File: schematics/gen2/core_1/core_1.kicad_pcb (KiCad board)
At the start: 2 copper layers, 84.3 x 8.4 mm, 10 parts, among them U1 74LS00, U2 74LS04, U3 74LS109, U4 74LS02

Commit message: core1 completed
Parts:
- added C1: C, Capacitor_THT:C_Disc_D5.0mm_W2.5mm_P2.50mm, F.Cu at (191.0, 79.2)
- added C10: C, Capacitor_THT:C_Disc_D5.0mm_W2.5mm_P2.50mm, F.Cu at (173.0, 38.2)
- added C11: C, Capacitor_THT:C_Disc_D5.0mm_W2.5mm_P2.50mm, F.Cu at (122.0, 71.7)
- added C12: C, Capacitor_THT:C_Disc_D5.0mm_W2.5mm_P2.50mm, F.Cu at (106.5, 71.4)
- added C16: C, Capacitor_THT:C_Disc_D5.0mm_W2.5mm_P2.50mm, F.Cu at (145.2, 102.8)
- added C2: C, Capacitor_THT:C_Disc_D5.0mm_W2.5mm_P2.50mm, F.Cu at (175.4, 78.3)
- added C3: C, Capacitor_THT:C_Disc_D5.0mm_W2.5mm_P2.50mm, F.Cu at (190.4, 52.9)
- added C4: C, Capacitor_THT:C_Disc_D5.0mm_W2.5mm_P2.50mm, F.Cu at (142.6, 39.0)
- added C5: C, Capacitor_THT:C_Radial_D6.3mm_H5.0mm_P2.50mm, F.Cu at (105.0, 117.5)
- added C9: C, Capacitor_THT:C_Disc_D5.0mm_W2.5mm_P2.50mm, F.Cu at (157.8, 39.5)
- added R1: 5kOhm, Resistor_THT:R_Axial_DIN0207_L6.3mm_D2.5mm_P7.62mm_Horizontal, F.Cu at (179.2, 102.6)
- moved INSTRUCTION1 72.1 mm to (144.6, 113.6), turned to 90 degrees
- moved DECODER2 70.2 mm to (161.4, 38.4)
- moved DECODER1 67.3 mm to (146.8, 38.4)
- moved U1 64.2 mm to (182.9, 57.0)
- moved U4 60.5 mm to (167.8, 82.2)
- moved U3 58.3 mm to (182.9, 82.4)
- moved DECODER4 54.5 mm to (98.9, 75.7)
- moved DECODER3 52.6 mm to (114.4, 75.7)
- moved BC1 47.9 mm to (103.0, 126.5)
- moved U2 16.8 mm to (130.9, 38.4)
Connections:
- U4 pad 11: Net-(R2-Pad2) -> Net-(U3A-~{S})
- U4 pad 12: Net-(R2-Pad2) -> Net-(U3A-~{S})
- U4 pad 8: Net-(R2-Pad2) -> Net-(U3A-~{S})
- U4 pad 9: Net-(R2-Pad2) -> Net-(U3A-~{S})
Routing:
- net /~{IntAck}: track 0.00 -> 277.5 mm, vias 0 -> 5
- net /~{ALUWriter}: track 0.00 -> 270.8 mm, vias 0 -> 5
- net /R4: track 0.00 -> 217.5 mm, vias 0 -> 5
- net Net-(DECODER3-E1): track 0.00 -> 164.7 mm, vias 0 -> 2
- net GND: track 0.00 -> 151.6 mm, vias 0 -> 7
- net /L0: track 0.00 -> 111.3 mm, vias 0 -> 2
- net Net-(BC1-STATE15): track 0.00 -> 110.6 mm, vias 0 -> 7
- net /L1: track 0.00 -> 108.5 mm, vias 0 -> 2
- net /~{InstructionReader}: track 0.00 -> 107.1 mm
- net /L2: track 0.00 -> 105.2 mm, vias 0 -> 2
- net /L3: track 0.00 -> 102.4 mm, vias 0 -> 2
- net /~{MemoryReader}: track 0.00 -> 101.4 mm, vias 0 -> 2
- net /IRQ: track 0.00 -> 94.5 mm, vias 0 -> 3
- net /SPHighReader: track 0.00 -> 92.1 mm, vias 0 -> 4
- net /STATE1: track 0.00 -> 89.8 mm, vias 0 -> 1
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- added copper zone on B.Cu, net GND
- added copper zone on F.Cu, net VCC
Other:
- board size 84.3 x 8.4 mm -> 100 x 91.1 mm

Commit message: design + fix core_2
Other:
- board text added: "CORE 2"

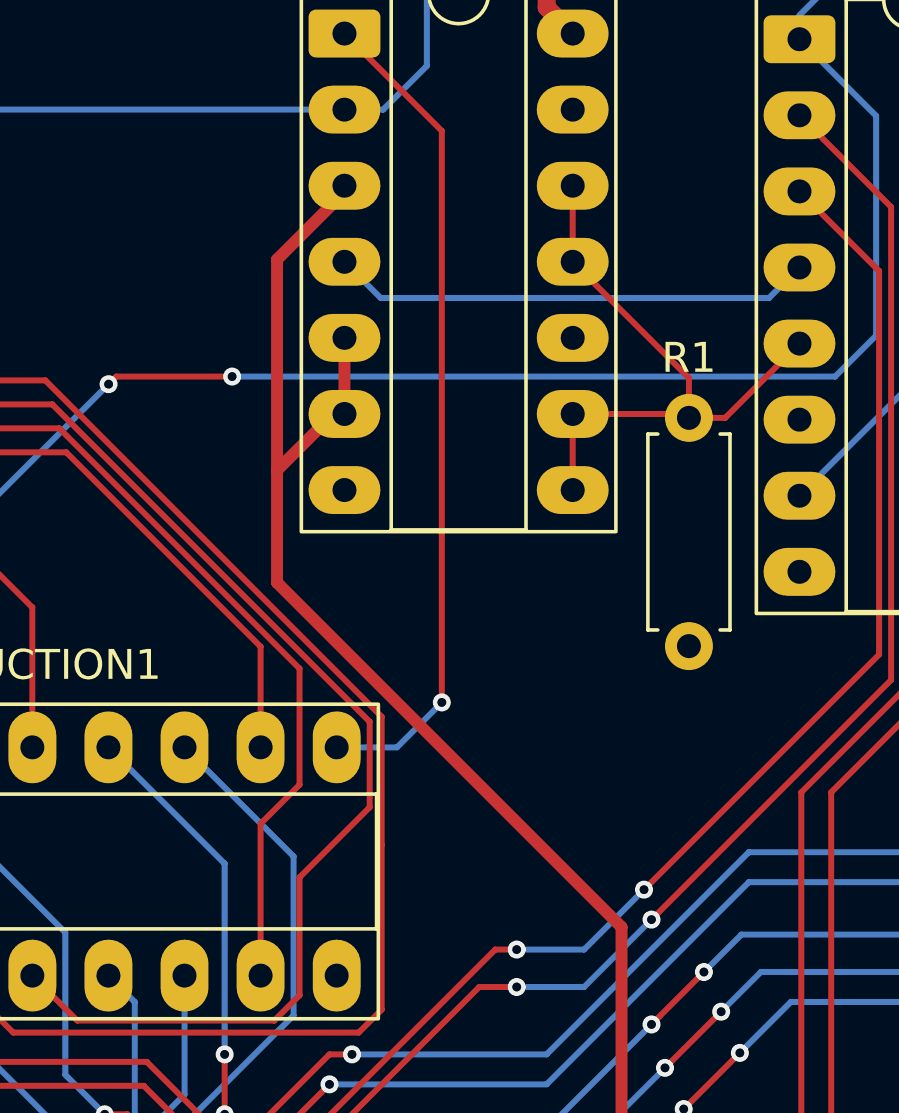
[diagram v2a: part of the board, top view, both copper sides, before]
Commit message: fix clk in core_1
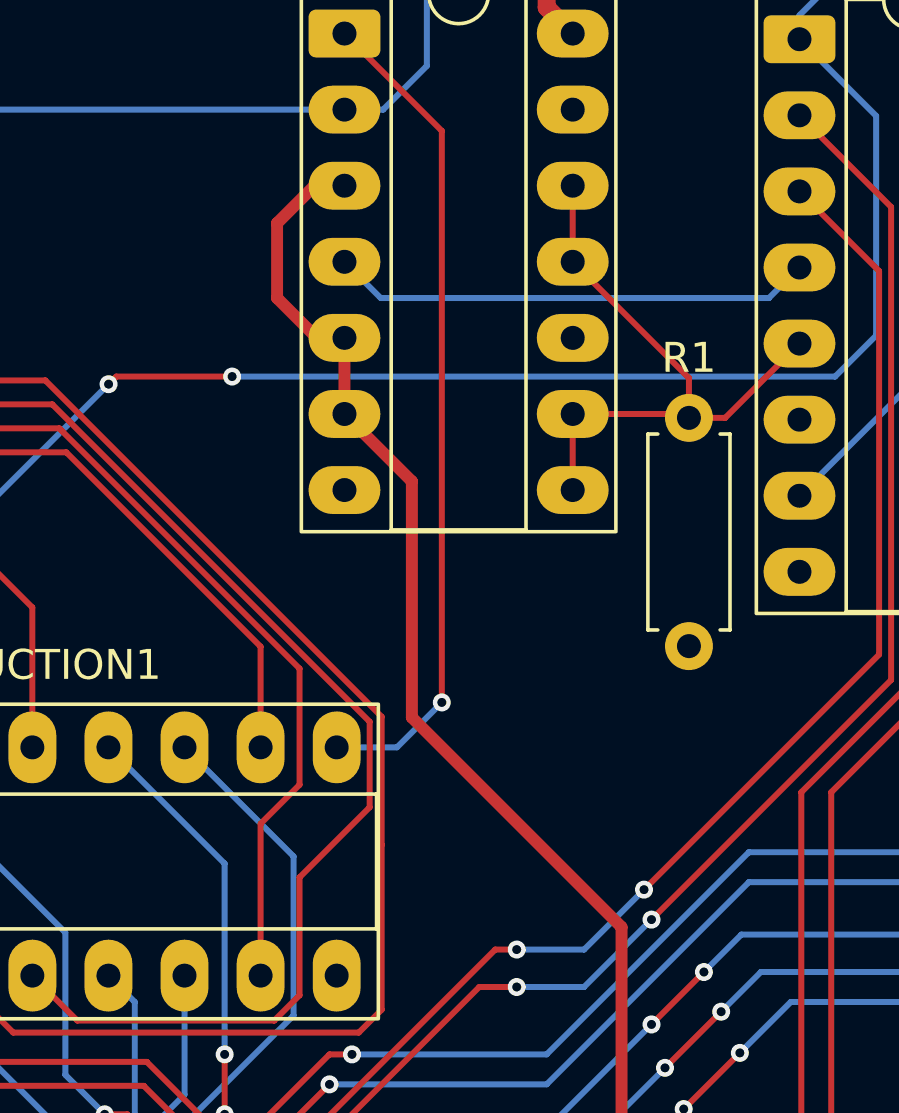
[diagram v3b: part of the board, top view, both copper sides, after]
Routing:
- net /~{Clk}: track 50.4 -> 46.4 mm
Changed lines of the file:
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@@
 	)
 	(segment
-		(start 165.5 89.713125)
-		(end 167.84472 87.368405)
+		(start 170 105)
+		(end 170 97.12)
 		(width 0.4)
 		(layer "F.Cu")
@@
 	)
 	(segment
-		(start 165.5 100.5)
-		(end 165.5 96.75)
+		(start 166.83 92.33)
+		(end 167.75 92.33)
 		(width 0.4)
 		(layer "F.Cu")
@@
 	)
 	(segment
-		(start 165.5 96.75)
-		(end 165.5 89.713125)
+		(start 165.5 88.5)
+		(end 165.5 91)
+		(width 0.4)
+		(layer "F.Cu")
+		(net 38)
+	)
+	(segment
+		(start 177 126.5)
+		(end 177 112)
+		(width 0.4)
+		(layer "F.Cu")
+		(net 38)
+	)
+	(segment
+		(start 167.75 87.25)
+		(end 166.75 87.25)
 		(width 0.4)
 		(layer "F.Cu")
@@
 	)
 	(segment
+		(start 165.5 91)
+		(end 166.83 92.33)
+		(width 0.4)
+		(layer "F.Cu")
+		(net 38)
+	)
+	(segment
+		(start 177 112)
+		(end 170 105)
+		(width 0.4)
+		(layer "F.Cu")
+		(net 38)
+	)
+	(segment
 		(start 167.75 94.87)
 		(end 167.75 92.33)
@@
 	)
 	(segment
-		(start 177 112)
-		(end 165.5 100.5)
+		(start 166.75 87.25)
+		(end 165.5 88.5)
 		(width 0.4)
 		(layer "F.Cu")
@@
 	)
 	(segment
-		(start 165.5 96.75)
-		(end 167.38 94.87)
+		(start 170 97.12)
+		(end 167.75 94.87)
 		(width 0.4)
 		(layer "F.Cu")
-		(net 38)
-	)
-	(segment
-		(start 177 126.5)
-		(end 177 112)
-		(width 0.4)
-		(layer "F.Cu")

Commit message: chore(core 1): added logo and text
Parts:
- added kibuzzard-6911CC41: G***, kibuzzard-6911CC41, F.Cu at (102.0, 35.6)
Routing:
- net VCC: track 61.7 -> 89.7 mm
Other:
- board text removed: "CORE 2"

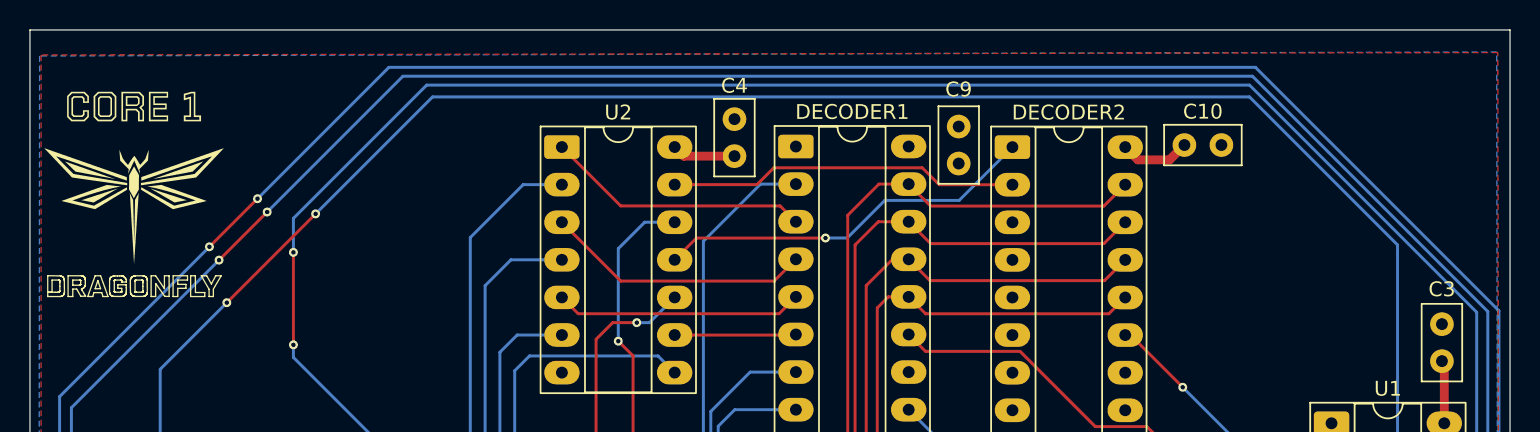
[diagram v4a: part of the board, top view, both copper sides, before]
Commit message: chore(kicad-pcb): added apps ucu logo
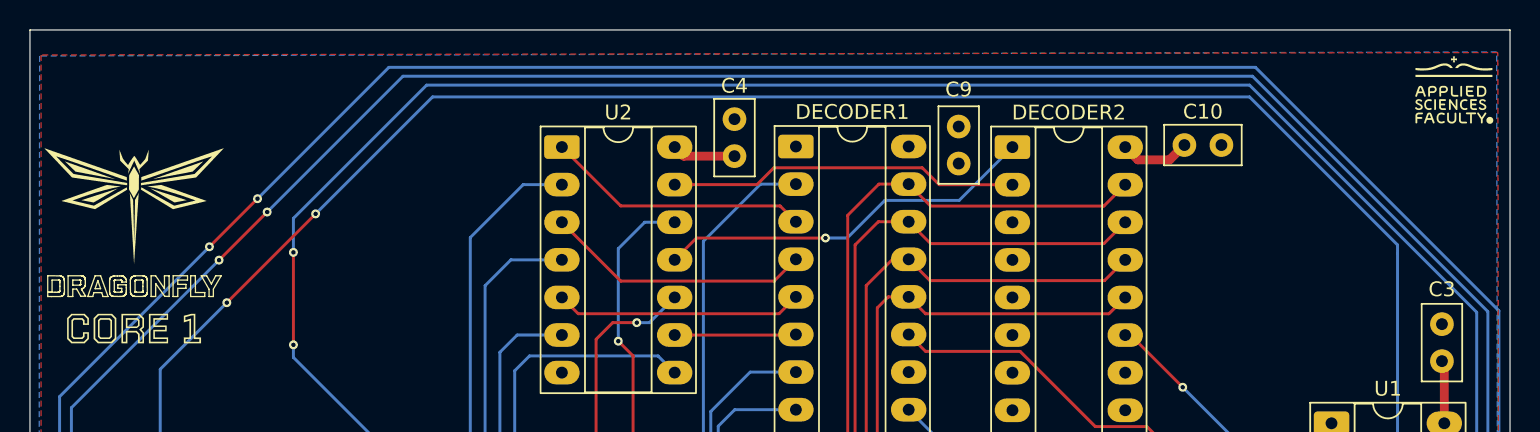
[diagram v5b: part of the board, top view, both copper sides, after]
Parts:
- moved kibuzzard-6911CC41 15.0 mm to (102.0, 50.6)

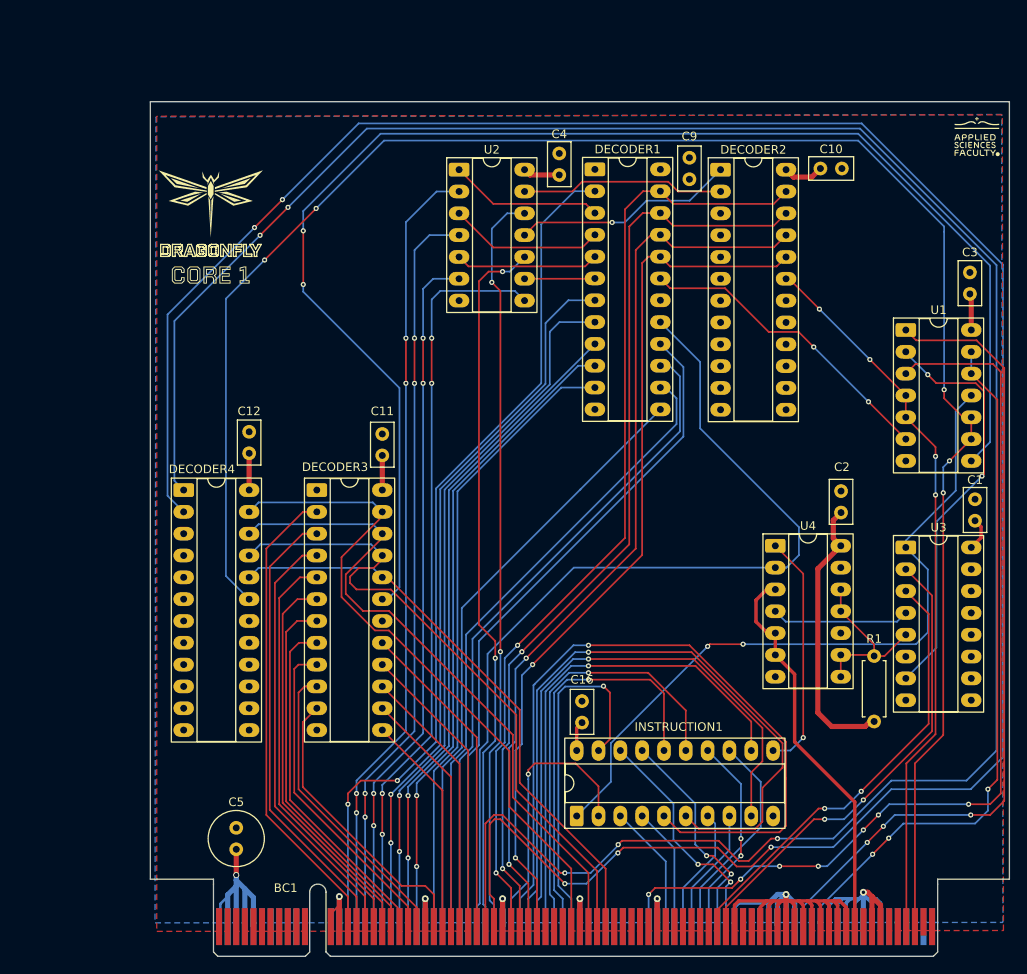
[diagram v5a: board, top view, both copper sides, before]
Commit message: fix(kicad): vcc zones
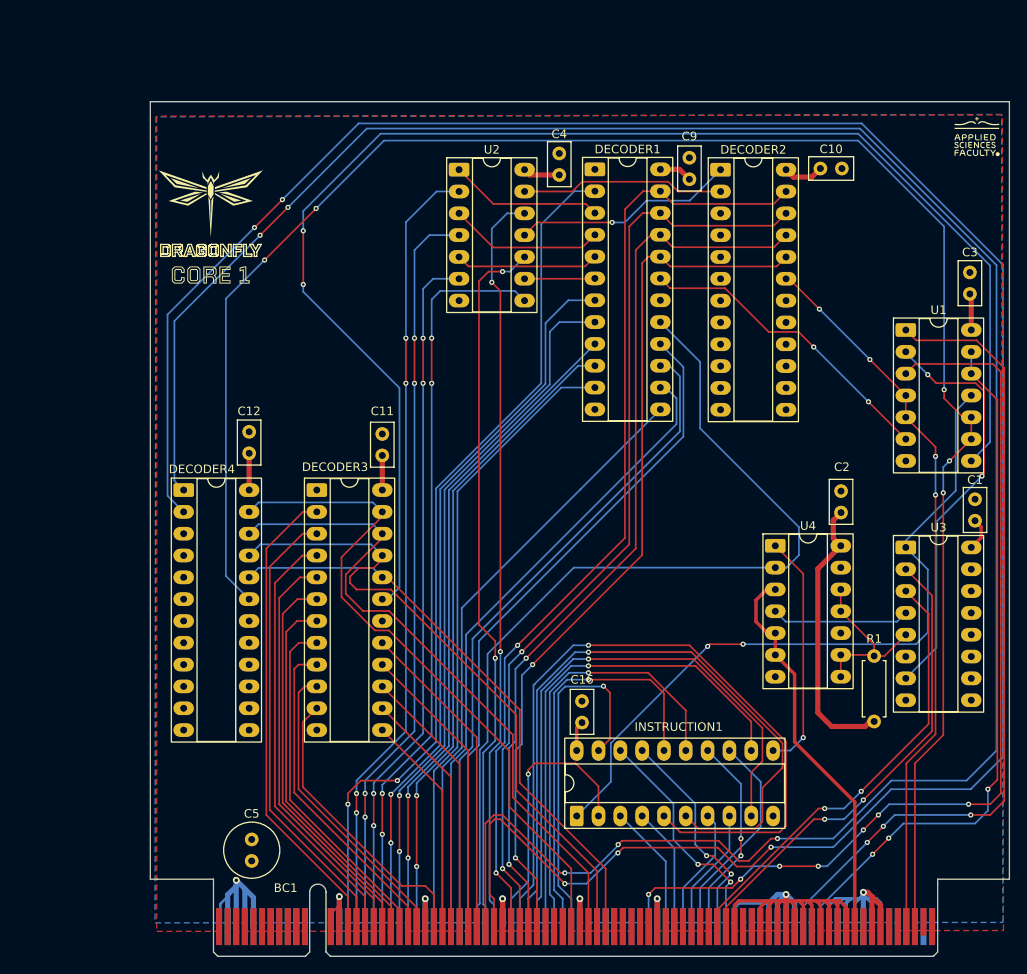
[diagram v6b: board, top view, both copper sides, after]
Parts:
- moved C5 2.25 mm to (106.8, 118.8)
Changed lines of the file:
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@@
 			(pinfunction "VCC")
 			(pintype "power_in")
+			(zone_connect 0)
 		)
 		(embedded_fonts no)
@@
 	(footprint "Capacitor_THT:C_Radial_D6.3mm_H5.0mm_P2.50mm"
 		(layer "F.Cu")
-		(at 105 117.5 90)
+		(at 106.8 118.85 90)
 		(descr "C, Radial series, Radial, pin pitch=2.50mm, diameter=6.3mm, height=5mm, Non-Polar Electrolytic Capacitor")
 		(tags "C Radial series Radial pin pitch 2.50mm diameter 6.3mm height 5mm Non-Polar Electrolytic Capacitor")
@@
 			(pinfunction "VCC")
 			(pintype "power_in")
+			(zone_connect 0)
 		)
 		(embedded_fonts no)
@@
 			(pinfunction "VCC")
 			(pintype "power_in")
+			(zone_connect 0)
 		)
 		(embedded_fonts no)
@@
 			(pinfunction "VCC")
 			(pintype "power_in")
+			(zone_connect 0)
 		)
 		(embedded_fonts no)
@@
 			(pinfunction "VCC")
 			(pintype "power_in")
+			(zone_connect 0)
 		)
 		(embedded_fonts no)
@@
 			(pinfunction "VCC")
 			(pintype "power_in")
+			(zone_connect 0)
 		)
 		(embedded_fonts no)
@@
 			(pinfunction "VCC")
 			(pintype "power_in")
+			(zone_connect 0)
 		)
 		(embedded_fonts no)
@@
 			(pinfunction "VCC")
 			(pintype "power_in")
+			(zone_connect 0)
 		)
 		(embedded_fonts no)
@@
 			(pinfunction "VCC")
 			(pintype "power_in")
+			(zone_connect 0)
 		)
 		(embedded_fonts no)
@@
 	)
 	(segment
-		(start 105 120.5)
-		(end 105 117.5)
-		(width 0.6)
-		(layer "F.Cu")
-		(net 2)
-	)
-	(segment
 		(start 190.56 57.05)
 		(end 190.56 53.01)
@@
 	)
 	(segment
+		(start 156.6 38.35)
+		(end 154.37 38.35)
+		(width 0.6)
+		(layer "F.Cu")
+		(net 2)
+	)
+	(segment
 		(start 172.7 84.84)
 		(end 172.7 101.6)
@@
 	)
 	(segment
+		(start 157.75 39.5)
+		(end 156.6 38.35)
+		(width 0.6)
+		(layer "F.Cu")
+		(net 2)
+	)
+	(segment
 		(start 169.86 39.25)
 		(end 172 39.25)
@@
 	)
 	(via
-		(at 105 120.5)
-		(size 0.7)
-		(drill 0.5)
+		(at 105 121.1)
+		(size 0.8)
+		(drill 0.4)
 		(layers "F.Cu" "B.Cu")
 		(free yes)
@@
 		(width 0.6)
 		(layer "B.Cu")
-		(net 2)
-	)
-	(segment
-		(start 105 120.5)
-		(end 105 121.1)
-		(width 0.6)
-		(layer "B.Cu")
